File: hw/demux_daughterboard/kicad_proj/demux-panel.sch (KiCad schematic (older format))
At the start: 23 parts, among them J1 DB37, J2 DB37, P1 CONN_5, P2 CONN_5, P3 CONN_6

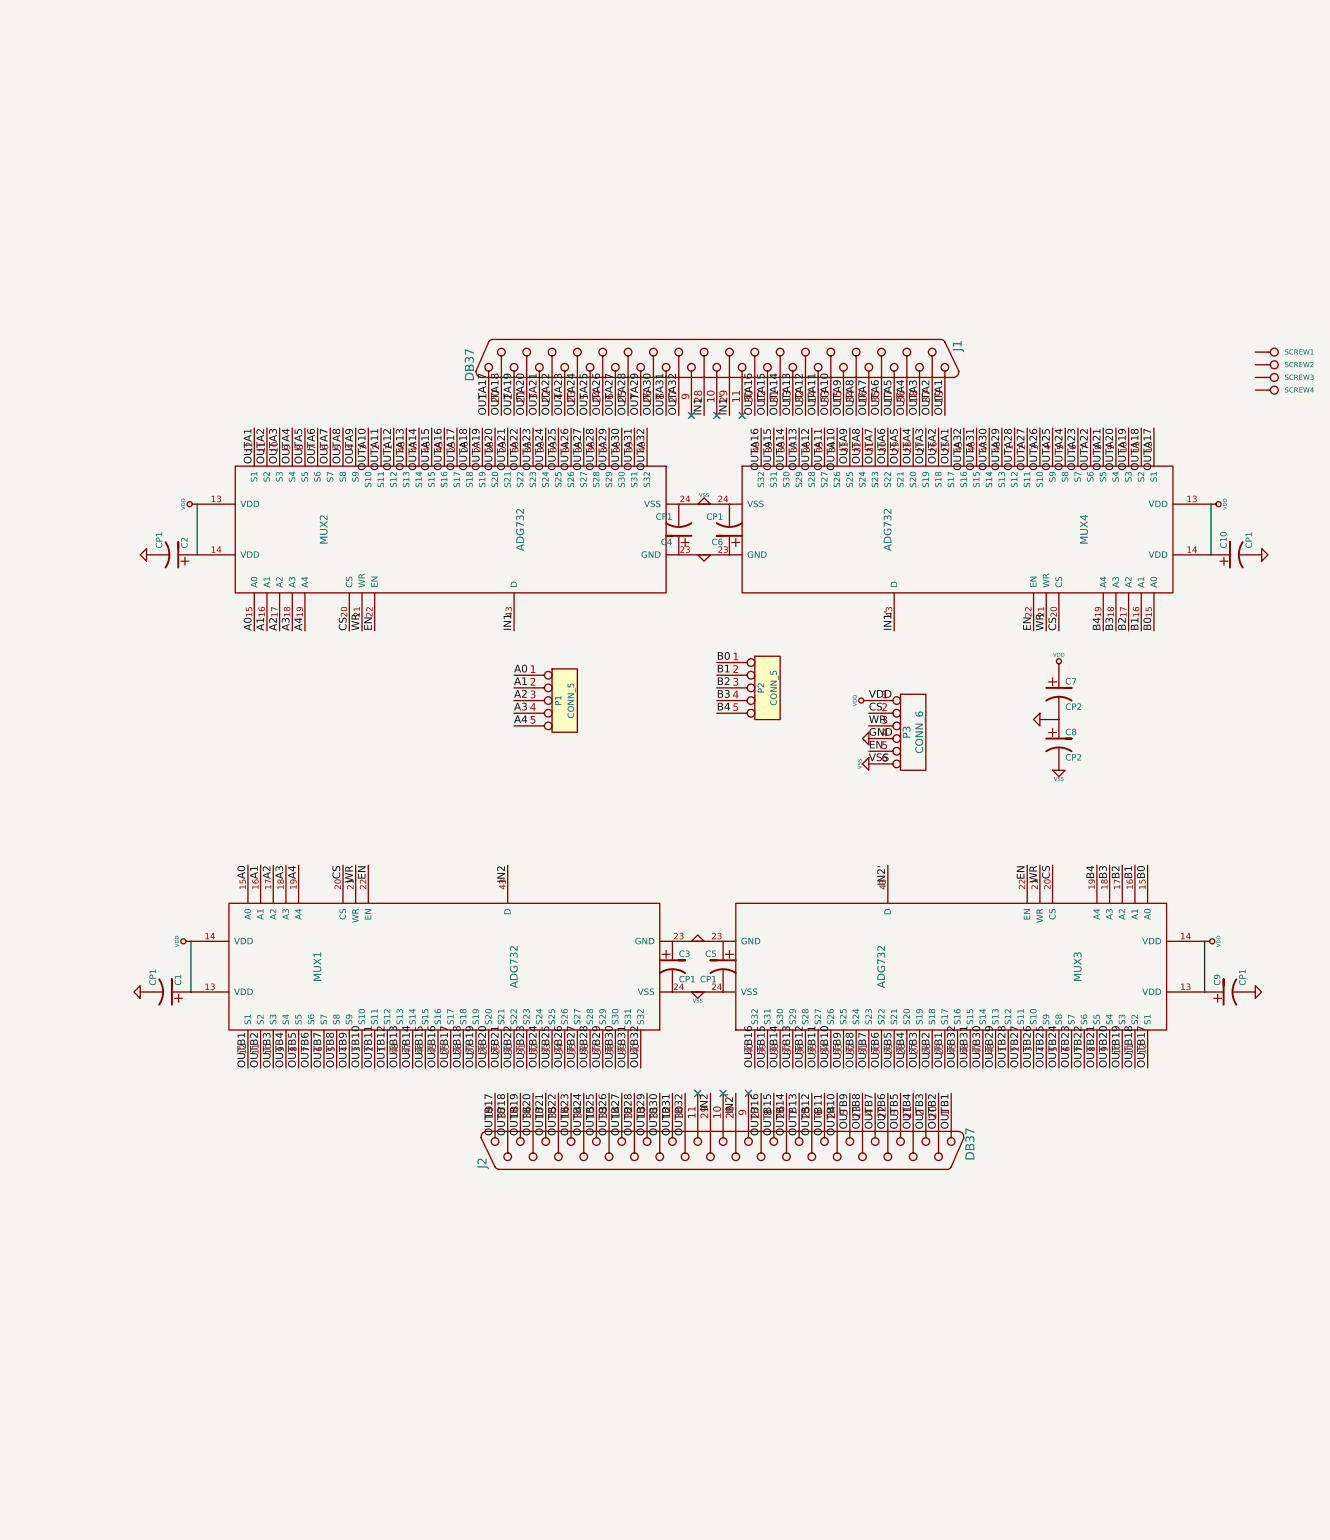
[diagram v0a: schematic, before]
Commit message: final rework of mux board, finalizing stacking connectors, almost there
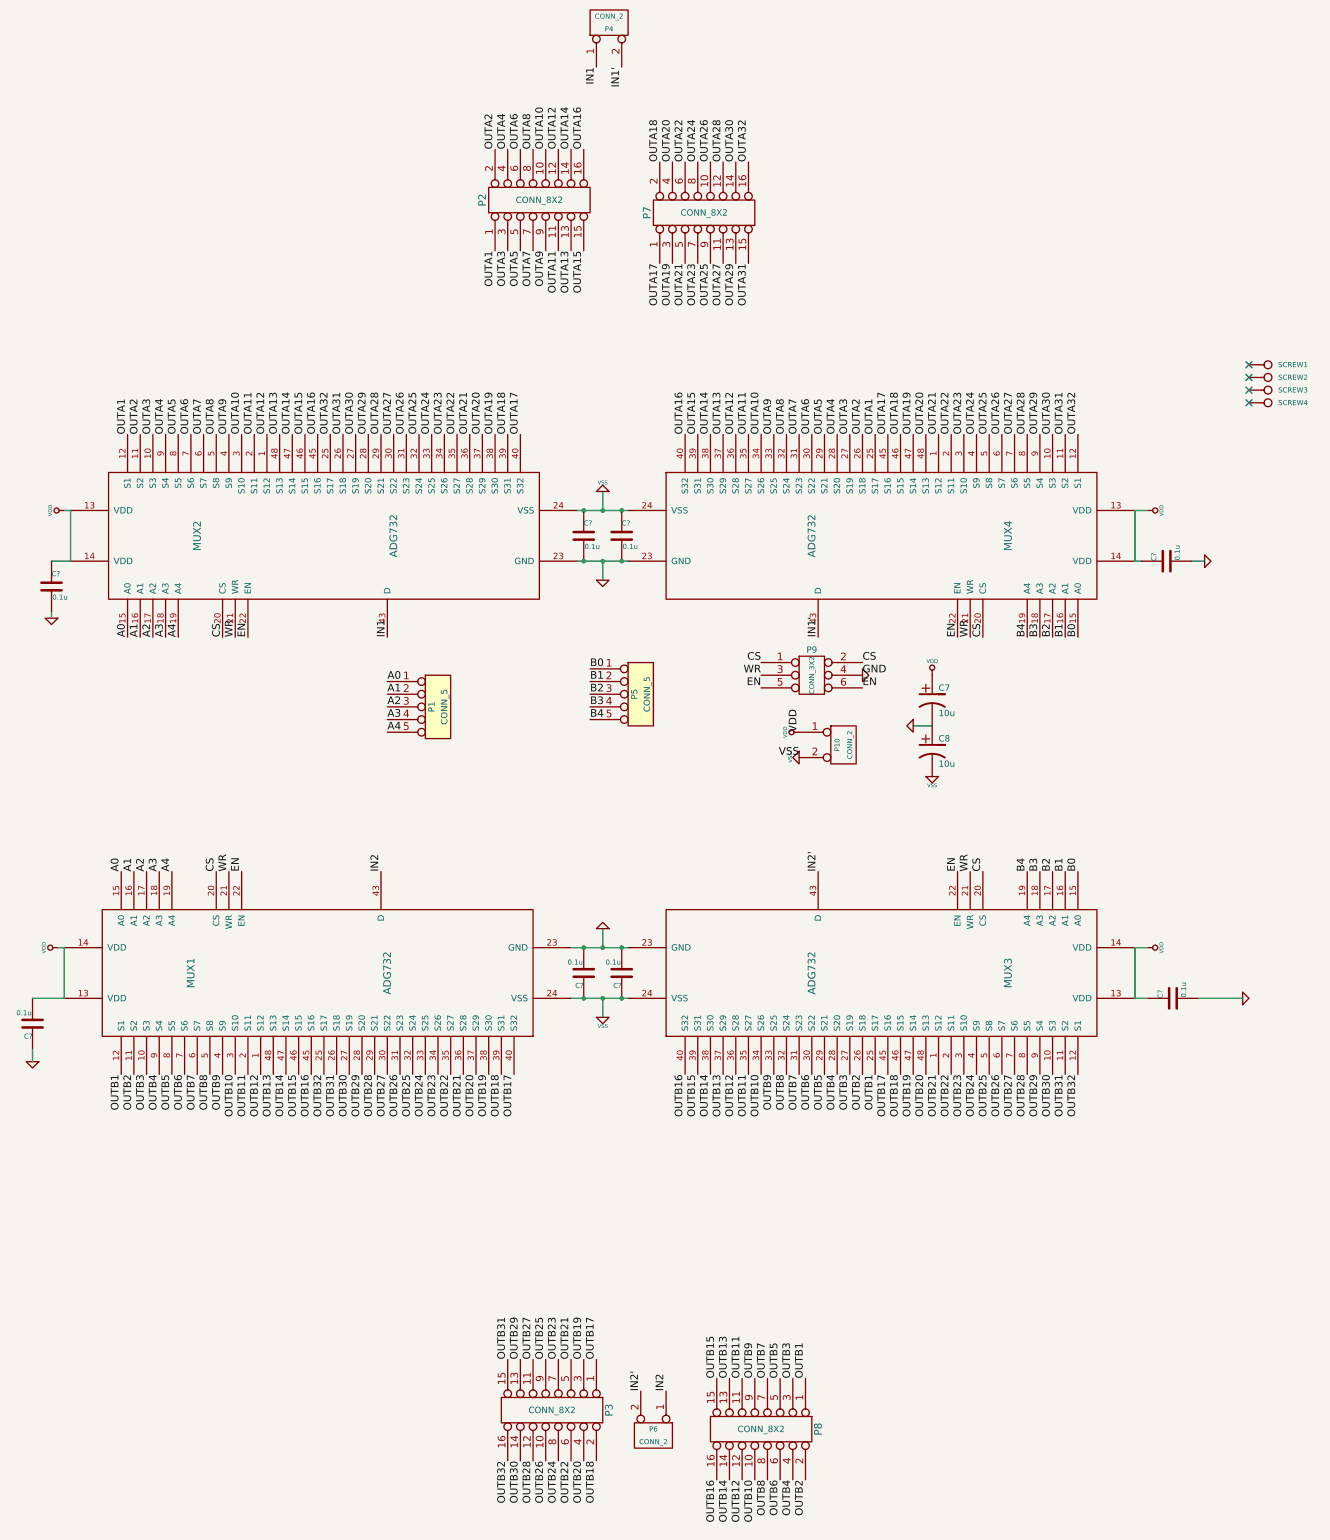
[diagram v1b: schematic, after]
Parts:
- removed C1, C10, C2, C3, C4, C5, C6, C9: CP1, symbol CP1
- removed J1, J2: DB37, symbol DB37
- removed P2: CONN_5, symbol CONN_5
- removed P3: CONN_6, symbol CONN_6
- added C? (x8): 0.1u, symbol C
- added P10, P4, P6: CONN_2, symbol CONN_2
- added P2, P3, P7, P8: CONN_8X2, symbol CONN_8X2
- added P5: CONN_5, symbol CONN_5
- added P9: CONN_3X2, symbol CONN_3X2
- C7, C8: value CP2 -> 10u
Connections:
- net B0: now also P5.1
- net B1: now also P5.2
- net B2: now also P5.3
- net B3: now also P5.4
- net B4: now also P5.5
- net CS: now also P9.1, P9.2
- net EN: now also P9.5, P9.6
- net GND: now also C?.1, C?.2, C?.2, C?.2, C?.2, C?.2, C?.2, C?.2, P9.4
- net IN1: now also P4.1 (P1)
- net IN1': now also P4.2 (PM)
- net IN2: now also P6.1 (P1)
- net IN2': now also P6.2 (PM)
- net OUTA1: now also P2.1
- net OUTA10: now also P2.10
- net OUTA11: now also P2.11
- net OUTA12: now also P2.12
- net OUTA13: now also P2.13
- net OUTA14: now also P2.14
- net OUTA15: now also P2.15
- net OUTA16: now also P2.16
- net OUTA17: now also MUX2.40 (S32), MUX4.45 (S16), P7.1; no longer MUX2.25 (S17), MUX4.12 (S1)
- net OUTA18: now also MUX2.39 (S31), MUX4.46 (S15), P7.2; no longer MUX2.26 (S18), MUX4.11 (S2)
- net OUTA19: now also MUX2.38 (S30), MUX4.47 (S14), P7.3; no longer MUX2.27 (S19), MUX4.10 (S3)
- net OUTA2: now also P2.2
- net OUTA20: now also MUX2.37 (S29), MUX4.48 (S13), P7.4; no longer MUX2.28 (S20), MUX4.9 (S4)
- net OUTA21: now also MUX2.36 (S28), MUX4.1 (S12), P7.5; no longer MUX2.29 (S21), MUX4.8 (S5)
- net OUTA22: now also MUX2.35 (S27), MUX4.2 (S11), P7.6; no longer MUX2.30 (S22), MUX4.7 (S6)
- net OUTA23: now also MUX2.34 (S26), MUX4.3 (S10), P7.7; no longer MUX2.31 (S23), MUX4.6 (S7)
- net OUTA24: now also MUX2.33 (S25), MUX4.4 (S9), P7.8; no longer MUX2.32 (S24), MUX4.5 (S8)
- net OUTA25: now also MUX2.32 (S24), MUX4.5 (S8), P7.9; no longer MUX2.33 (S25), MUX4.4 (S9)
- net OUTA26: now also MUX2.31 (S23), MUX4.6 (S7), P7.10; no longer MUX2.34 (S26), MUX4.3 (S10)
- net OUTA27: now also MUX2.30 (S22), MUX4.7 (S6), P7.11; no longer MUX2.35 (S27), MUX4.2 (S11)
- net OUTA28: now also MUX2.29 (S21), MUX4.8 (S5), P7.12; no longer MUX2.36 (S28), MUX4.1 (S12)
- net OUTA29: now also MUX2.28 (S20), MUX4.9 (S4), P7.13; no longer MUX2.37 (S29), MUX4.48 (S13)
- net OUTA3: now also P2.3
- net OUTA30: now also MUX2.27 (S19), MUX4.10 (S3), P7.14; no longer MUX2.38 (S30), MUX4.47 (S14)
- net OUTA31: now also MUX2.26 (S18), MUX4.11 (S2), P7.15; no longer MUX2.39 (S31), MUX4.46 (S15)
- net OUTA32: now also MUX2.25 (S17), MUX4.12 (S1), P7.16; no longer MUX2.40 (S32), MUX4.45 (S16)
- net OUTA4: now also P2.4
- net OUTA5: now also P2.5
- net OUTA6: now also P2.6
- net OUTA7: now also P2.7
- net OUTA8: now also P2.8
- net OUTA9: now also P2.9
- net OUTB1: now also P8.1
- net OUTB10: now also P8.10
- net OUTB11: now also P8.11
- net OUTB12: now also P8.12
- net OUTB13: now also P8.13
- net OUTB14: now also P8.14
- net OUTB15: now also P8.15
- net OUTB16: now also P8.16
- net OUTB17: now also MUX1.40 (S32), MUX3.45 (S16), P3.1; no longer MUX1.25 (S17), MUX3.12 (S1)
- net OUTB18: now also MUX1.39 (S31), MUX3.46 (S15), P3.2; no longer MUX1.26 (S18), MUX3.11 (S2)
- net OUTB19: now also MUX1.38 (S30), MUX3.47 (S14), P3.3; no longer MUX1.27 (S19), MUX3.10 (S3)
- net OUTB2: now also P8.2
- net OUTB20: now also MUX1.37 (S29), MUX3.48 (S13), P3.4; no longer MUX1.28 (S20), MUX3.9 (S4)
- net OUTB21: now also MUX1.36 (S28), MUX3.1 (S12), P3.5; no longer MUX1.29 (S21), MUX3.8 (S5)
- net OUTB22: now also MUX1.35 (S27), MUX3.2 (S11), P3.6; no longer MUX1.30 (S22), MUX3.7 (S6)
- net OUTB23: now also MUX1.34 (S26), MUX3.3 (S10), P3.7; no longer MUX1.31 (S23), MUX3.6 (S7)
- net OUTB24: now also MUX1.33 (S25), MUX3.4 (S9), P3.8; no longer MUX1.32 (S24), MUX3.5 (S8)
- net OUTB25: now also MUX1.32 (S24), MUX3.5 (S8), P3.9; no longer MUX1.33 (S25), MUX3.4 (S9)
- net OUTB26: now also MUX1.31 (S23), MUX3.6 (S7), P3.10; no longer MUX1.34 (S26), MUX3.3 (S10)
- net OUTB27: now also MUX1.30 (S22), MUX3.7 (S6), P3.11; no longer MUX1.35 (S27), MUX3.2 (S11)
- net OUTB28: now also MUX1.29 (S21), MUX3.8 (S5), P3.12; no longer MUX1.36 (S28), MUX3.1 (S12)
- net OUTB29: now also MUX1.28 (S20), MUX3.9 (S4), P3.13; no longer MUX1.37 (S29), MUX3.48 (S13)
- net OUTB3: now also P8.3
- net OUTB30: now also MUX1.27 (S19), MUX3.10 (S3), P3.14; no longer MUX1.38 (S30), MUX3.47 (S14)
- net OUTB31: now also MUX1.26 (S18), MUX3.11 (S2), P3.15; no longer MUX1.39 (S31), MUX3.46 (S15)
- net OUTB32: now also MUX1.25 (S17), MUX3.12 (S1), P3.16; no longer MUX1.40 (S32), MUX3.45 (S16)
- net OUTB4: now also P8.4
- net OUTB5: now also P8.5
- net OUTB6: now also P8.6
- net OUTB7: now also P8.7
- net OUTB8: now also P8.8
- net OUTB9: now also P8.9
- net VDD: now also C?.1, C?.1, C?.1, C?.2, P10.1 (P1)
- net VSS: now also C?.1, C?.1, C?.1, C?.1, P10.2 (PM)
- net WR: now also P9.3
- no-connect marks 6 -> 4
